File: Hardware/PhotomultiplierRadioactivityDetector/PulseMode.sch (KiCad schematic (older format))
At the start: 15 parts

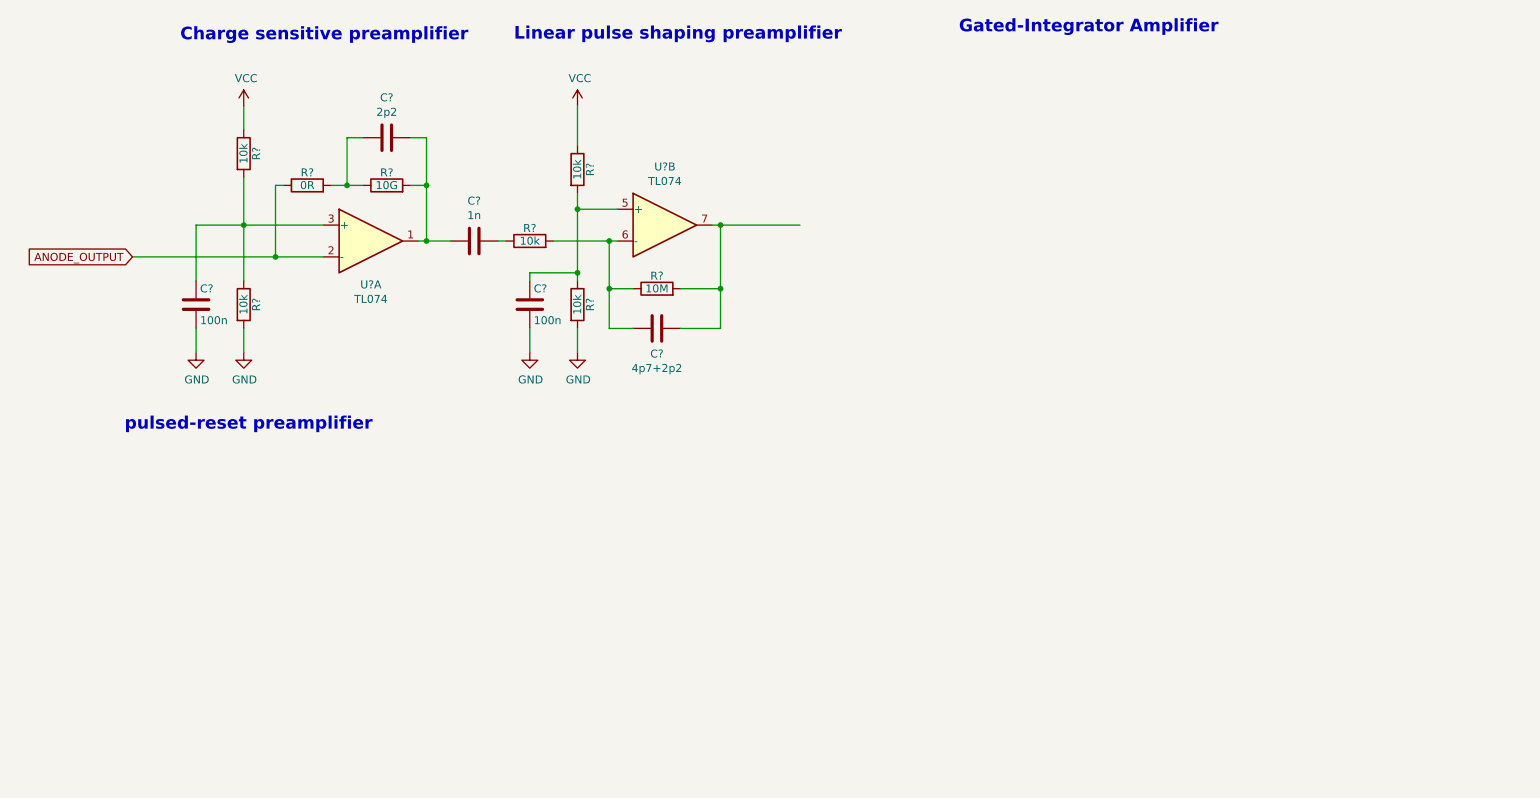
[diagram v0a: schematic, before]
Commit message: add resetable charge amplifier to circuit schemat
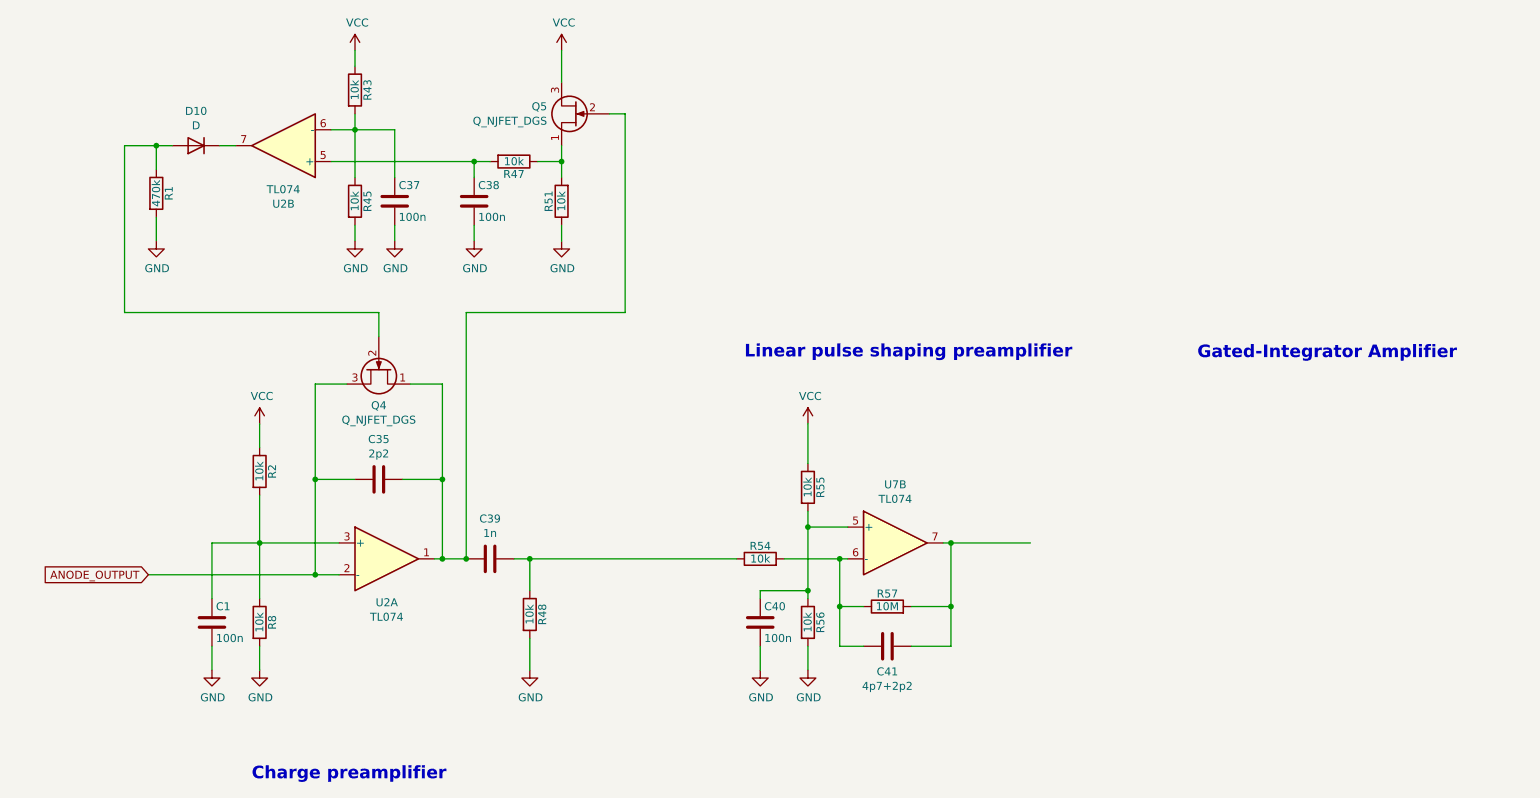
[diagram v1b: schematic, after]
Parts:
- removed R?: 10G, Resistor_SMD:R_0805_2012Metric_Pad1.15x1.40mm_HandSolder, symbol Device:R
- removed R?: 0R, Resistor_SMD:R_0805_2012Metric_Pad1.15x1.40mm_HandSolder, symbol Device:R
- added C37, C38: 100n, Capacitor_SMD:C_0805_2012Metric_Pad1.15x1.40mm_HandSolder, symbol Device:C
- added D10: D, symbol Device:D
- added Q4, Q5: Q_NJFET_DGS, symbol Device:Q_NJFET_DGS
- added R1: 470k, Resistor_SMD:R_0805_2012Metric_Pad1.15x1.40mm_HandSolder, symbol Device:R
- added R43, R45, R47, R48, R51: 10k, Resistor_SMD:R_0805_2012Metric_Pad1.15x1.40mm_HandSolder, symbol Device:R
- added unit 2 of U2
- gave numbers to parts that had none: 13
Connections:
- net ANODE_OUTPUT: now also C35.2, Q4.3 (S)
- net GND: now also C37.2, C38.2, R1.2, R45.2, R48.2, R51.1
- net VCC: now also Q5.3 (S), R43.1
- net at C35.1, C39.2, U2.1: now also Q4.1 (D), Q5.2 (G)
- net at C39.1, R54.1: now also R48.1
- new net: D10.2 (A), Q4.2 (G), R1.1
- new net: C38.1, R47.2, U2.5 (+)
- new net: C37.1, R43.2, R45.1, U2.6 (-)
- new net: D10.1 (K), U2.7
- new net: Q5.1 (D), R47.1, R51.2
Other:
- note added: "Charge preamplifier\n"
- note removed: "Charge sensitive preamplifier\n"
- note removed: "pulsed-reset preamplifier\n"
- moved on the sheet: C1, C35, C39, C40, C41, R2, R54, R55, R56, R57, R8, U2A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
